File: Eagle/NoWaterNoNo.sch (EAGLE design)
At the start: 13 parts, among them U2 TINY85-20-DIP

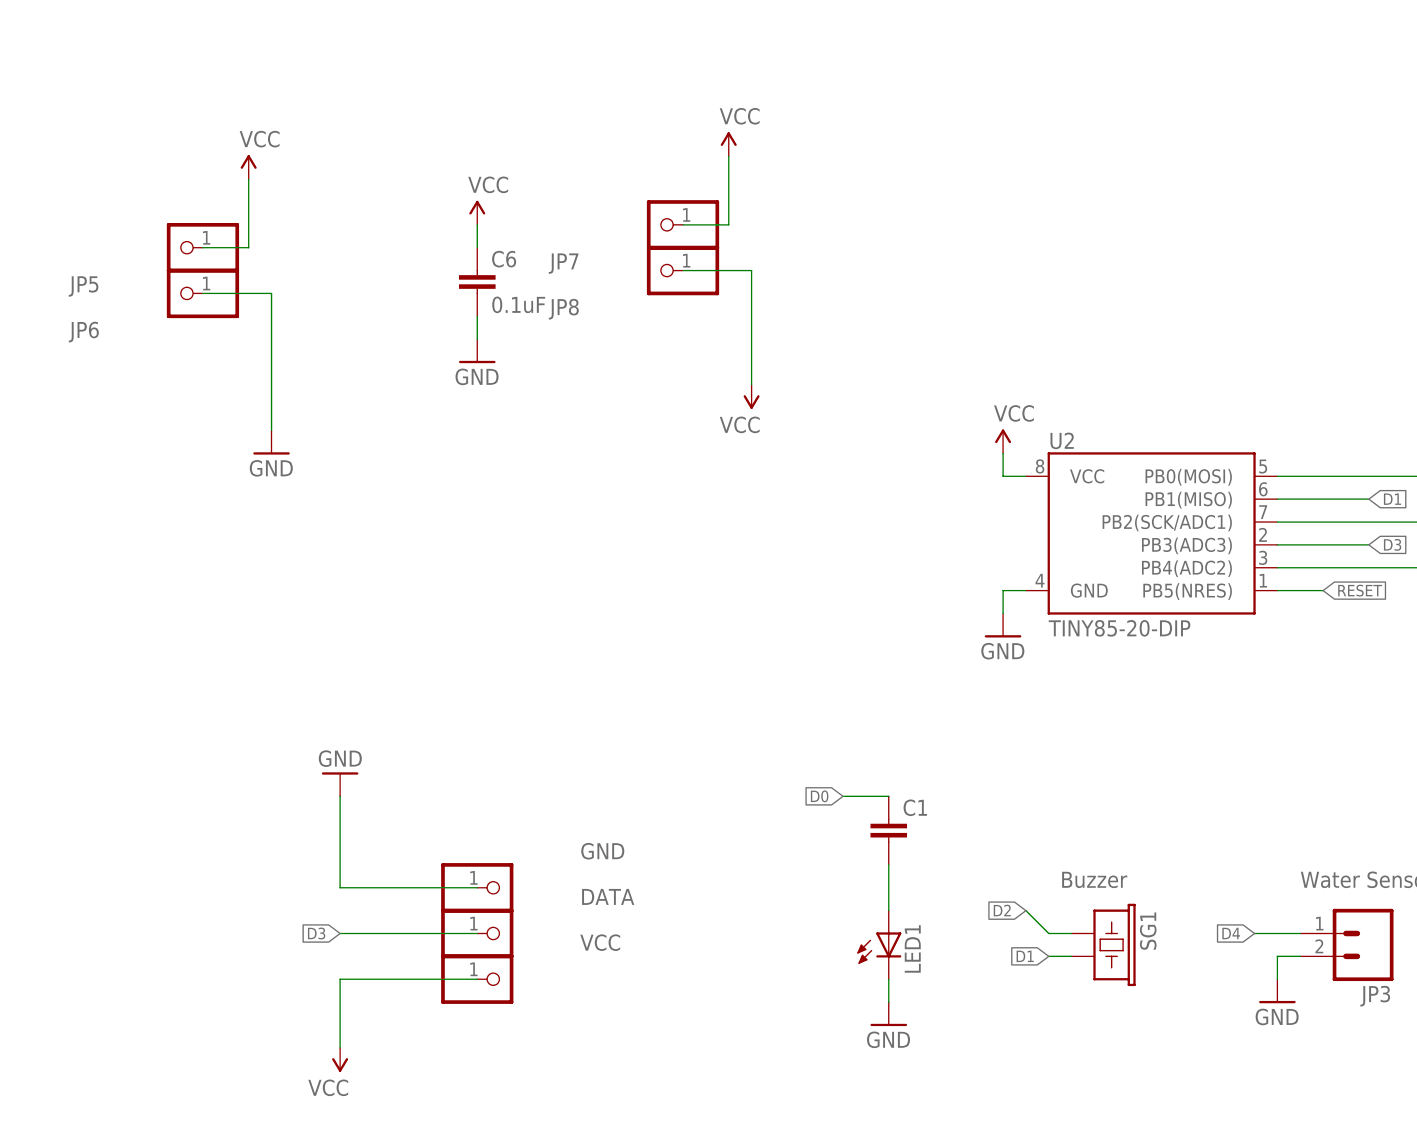
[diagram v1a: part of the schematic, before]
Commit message: Changed board layout. Buzzer, radio and sensor have changed pin assignments.
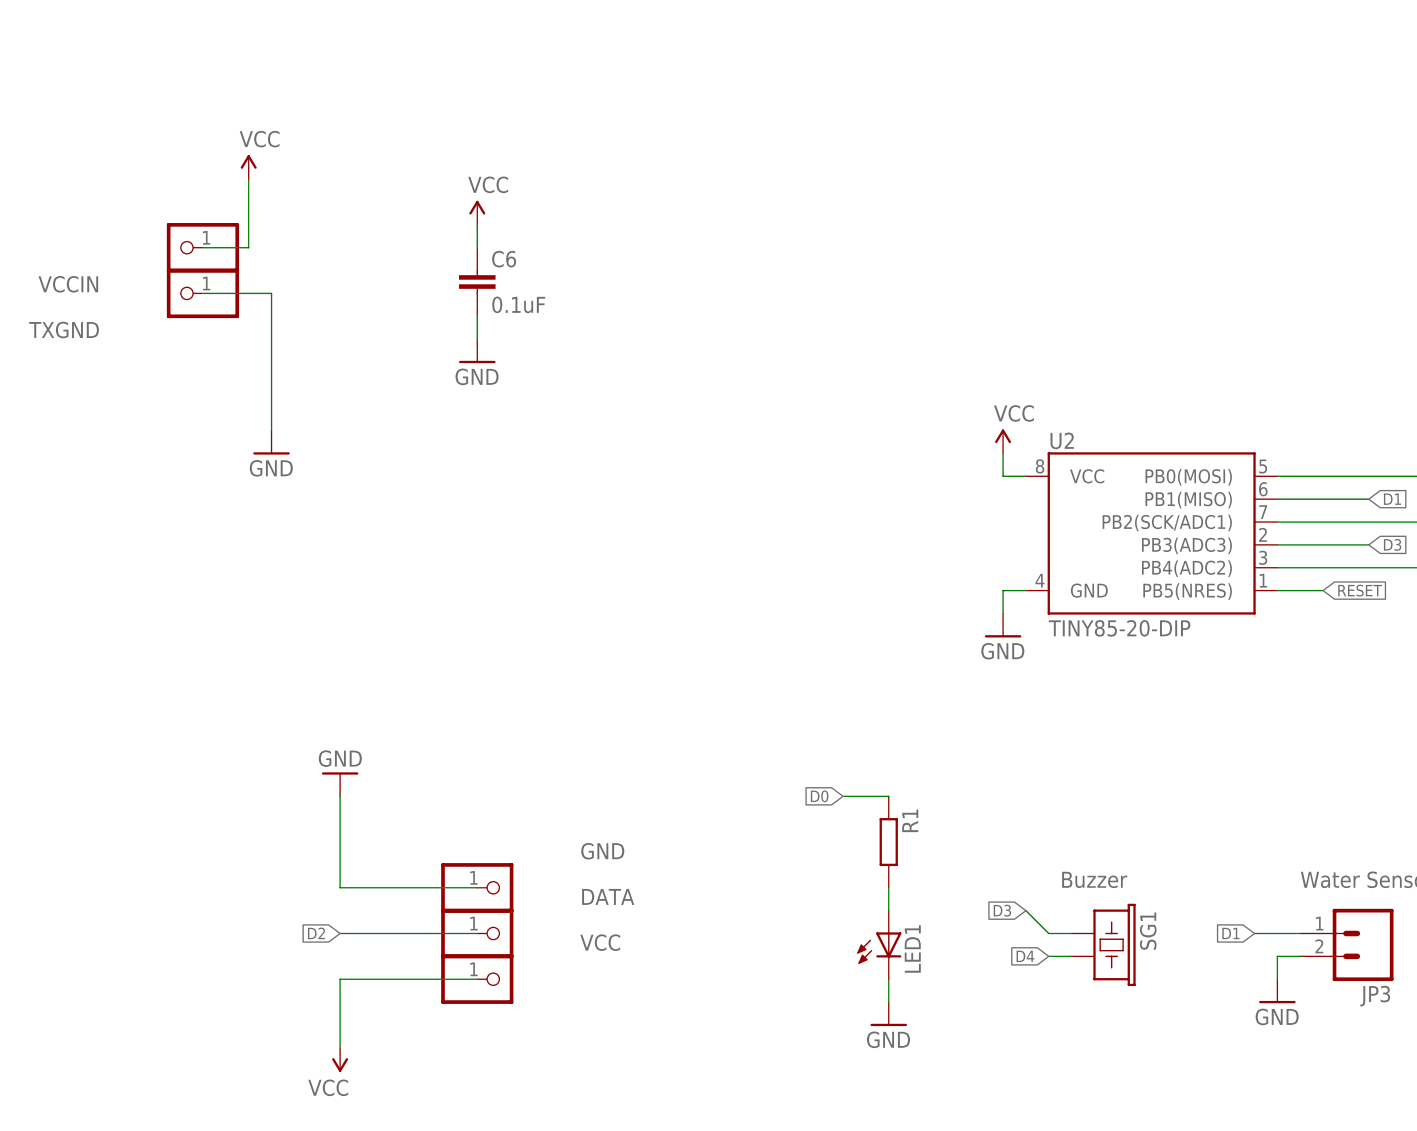
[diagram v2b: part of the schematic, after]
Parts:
- removed C1: (no value), resistor:C-EU025-025X050
- removed JP7, JP8: (no value), pinhead:PINHD-1X1
- added R1: (no value), rcl:R-EU_0204/2V
- renumbered JP5 to VCCIN, JP6 to TXGND
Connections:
- net D0: now also R1.1; no longer C1.1
- net D1: now also JP3.1; no longer SG1.2
- net D2: now also DATA.1; no longer SG1.1
- net D3: now also SG1.1; no longer DATA.1
- net D4: now also SG1.2; no longer JP3.1
- net N$1: now also R1.2; no longer C1.2
- net VCC: no longer JP7.1, JP8.1
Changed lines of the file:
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@@
 <part name="GND1" library="SparkFun" deviceset="GND" device=""/>
 <part name="P+1" library="SparkFun" deviceset="VCC" device=""/>
-<part name="JP5" library="pinhead" deviceset="PINHD-1X1" device=""/>
-<part name="JP6" library="pinhead" deviceset="PINHD-1X1" device=""/>
-<part name="P+4" library="SparkFun" deviceset="VCC" device=""/>
-<part name="JP7" library="pinhead" deviceset="PINHD-1X1" device=""/>
-<part name="JP8" library="pinhead" deviceset="PINHD-1X1" device=""/>
-<part name="P+6" library="SparkFun" deviceset="VCC" device=""/>
-<part name="C1" library="resistor" deviceset="C-EU" device="025-025X050"/>
+<part name="VCCIN" library="pinhead" deviceset="PINHD-1X1" device=""/>
+<part name="TXGND" library="pinhead" deviceset="PINHD-1X1" device=""/>
+<part name="R1" library="rcl" deviceset="R-EU_" device="0204/2V"/>
 </parts>
 <sheets>
@@
 <instance part="GND1" gate="1" x="48.26" y="99.06" rot="R180"/>
 <instance part="P+1" gate="1" x="48.26" y="68.58" rot="R180"/>
-<instance part="JP5" gate="G$1" x="30.48" y="157.48" smashed="yes" rot="R180">
+<instance part="VCCIN" gate="G$1" x="30.48" y="157.48" smashed="yes" rot="R180">
 <attribute name="NAME" x="21.59" y="154.305" size="1.778" layer="95" rot="R180"/>
 <attribute name="VALUE" x="36.83" y="162.56" size="1.778" layer="96" rot="R180"/>
 </instance>
-<instance part="JP6" gate="G$1" x="30.48" y="152.4" smashed="yes" rot="R180">
+<instance part="TXGND" gate="G$1" x="30.48" y="152.4" smashed="yes" rot="R180">
 <attribute name="NAME" x="21.59" y="149.225" size="1.778" layer="95" rot="R180"/>
 <attribute name="VALUE" x="36.83" y="157.48" size="1.778" layer="96" rot="R180"/>
 </instance>
-<instance part="P+4" gate="1" x="91.44" y="167.64"/>
-<instance part="JP7" gate="G$1" x="83.82" y="160.02" smashed="yes" rot="R180">
-<attribute name="NAME" x="74.93" y="156.845" size="1.778" layer="95" rot="R180"/>
-<attribute name="VALUE" x="90.17" y="165.1" size="1.778" layer="96" rot="R180"/>
-</instance>
-<instance part="JP8" gate="G$1" x="83.82" y="154.94" smashed="yes" rot="R180">
-<attribute name="NAME" x="74.93" y="151.765" size="1.778" layer="95" rot="R180"/>
-<attribute name="VALUE" x="90.17" y="160.02" size="1.778" layer="96" rot="R180"/>
-</instance>
-<instance part="P+6" gate="1" x="93.98" y="142.24" rot="R180"/>
-<instance part="C1" gate="G$1" x="109.22" y="93.98"/>
+<instance part="R1" gate="G$1" x="109.22" y="91.44" rot="R270"/>
 </instances>
 <busses>
@@
 <segment>
 <pinref part="GND7" gate="1" pin="GND"/>
-<pinref part="JP6" gate="G$1" pin="1"/>
+<pinref part="TXGND" gate="G$1" pin="1"/>
 <wire x1="33.02" y1="152.4" x2="40.64" y2="152.4" width="0.1524" layer="91"/>
 <wire x1="40.64" y1="152.4" x2="40.64" y2="137.16" width="0.1524" layer="91"/>
@@
 <pinref part="P+2" gate="1" pin="VCC"/>
 <wire x1="38.1" y1="165.1" x2="38.1" y2="157.48" width="0.1524" layer="91"/>
-<pinref part="JP5" gate="G$1" pin="1"/>
+<pinref part="VCCIN" gate="G$1" pin="1"/>
 <wire x1="38.1" y1="157.48" x2="33.02" y2="157.48" width="0.1524" layer="91"/>
 </segment>
@@
 <wire x1="48.26" y1="76.2" x2="48.26" y2="68.58" width="0.1524" layer="91"/>
 </segment>
-<segment>
-<pinref part="P+4" gate="1" pin="VCC"/>
-<wire x1="91.44" y1="167.64" x2="91.44" y2="160.02" width="0.1524" layer="91"/>
-<pinref part="JP7" gate="G$1" pin="1"/>
-<wire x1="91.44" y1="160.02" x2="86.36" y2="160.02" width="0.1524" layer="91"/>
-</segment>
-<segment>
-<pinref part="JP8" gate="G$1" pin="1"/>
-<wire x1="86.36" y1="154.94" x2="93.98" y2="154.94" width="0.1524" layer="91"/>
-<wire x1="93.98" y1="154.94" x2="93.98" y2="142.24" width="0.1524" layer="91"/>
-<pinref part="P+6" gate="1" pin="VCC"/>
-</segment>
 </net>
 <net name="RESET" class="0">
@@
 <net name="D4" class="0">
 <segment>
-<pinref part="JP3" gate="G$1" pin="1"/>
-<wire x1="154.94" y1="81.28" x2="149.86" y2="81.28" width="0.1524" layer="91"/>
-<label x="149.86" y="81.28" size="1.27" layer="95" rot="R180" xref="yes"/>
-</segment>
-<segment>
 <pinref part="U2" gate="G$1" pin="PB4(ADC2)"/>
 <wire x1="152.4" y1="121.92" x2="170.18" y2="121.92" width="0.1524" layer="91"/>
 <label x="170.18" y="121.92" size="1.27" layer="95" xref="yes"/>
 </segment>
+<segment>
+<pinref part="SG1" gate="G$1" pin="2"/>
+<wire x1="129.54" y1="78.74" x2="127" y2="78.74" width="0.1524" layer="91"/>
+<label x="127" y="78.74" size="1.27" layer="95" rot="R180" xref="yes"/>
+</segment>
 </net>
 <net name="D0" class="0">
@@
 <label x="104.14" y="96.52" size="1.27" layer="95" rot="R180" xref="yes"/>
 <wire x1="104.14" y1="96.52" x2="109.22" y2="96.52" width="0.1524" layer="91"/>
-<pinref part="C1" gate="G$1" pin="1"/>
-</segment>
-</net>
-<net name="D1" class="0">
-<segment>
-<pinref part="SG1" gate="G$1" pin="2"/>
-<wire x1="129.54" y1="78.74" x2="127" y2="78.74" width="0.1524" layer="91"/>
-<label x="127" y="78.74" size="1.27" layer="95" rot="R180" xref="yes"/>
-</segment>
-<segment>
-<pinref part="U2" gate="G$1" pin="PB1(MISO)"/>
-<wire x1="152.4" y1="129.54" x2="162.56" y2="129.54" width="0.1524" layer="91"/>
-<label x="162.56" y="129.54" size="1.27" layer="95" xref="yes"/>
-</segment>
-</net>
-<net name="D2" class="0">
-<segment>
-<pinref part="U2" gate="G$1" pin="PB2(SCK/ADC1)"/>
-<wire x1="152.4" y1="127" x2="170.18" y2="127" width="0.1524" layer="91"/>
-<label x="170.18" y="127" size="1.27" layer="95" xref="yes"/>
+<pinref part="R1" gate="G$1" pin="1"/>
+</segment>
+</net>
+<net name="D3" class="0">
+<segment>
+<pinref part="U2" gate="G$1" pin="PB3(ADC3)"/>
+<wire x1="152.4" y1="124.46" x2="162.56" y2="124.46" width="0.1524" layer="91"/>
+<label x="162.56" y="124.46" size="1.27" layer="95" xref="yes"/>
 </segment>
 <segment>
@@
 </segment>
 </net>
-<net name="D3" class="0">
-<segment>
-<pinref part="U2" gate="G$1" pin="PB3(ADC3)"/>
-<wire x1="152.4" y1="124.46" x2="162.56" y2="124.46" width="0.1524" layer="91"/>
-<label x="162.56" y="124.46" size="1.27" layer="95" xref="yes"/>
+<net name="N$1" class="0">
+<segment>
+<pinref part="R1" gate="G$1" pin="2"/>
+<pinref part="LED1" gate="G$1" pin="A"/>
+<wire x1="109.22" y1="86.36" x2="109.22" y2="83.82" width="0.1524" layer="91"/>
+</segment>
+</net>
+<net name="D1" class="0">
+<segment>
+<pinref part="U2" gate="G$1" pin="PB1(MISO)"/>
+<wire x1="152.4" y1="129.54" x2="162.56" y2="129.54" width="0.1524" layer="91"/>
+<label x="162.56" y="129.54" size="1.27" layer="95" xref="yes"/>
+</segment>
+<segment>
+<pinref part="JP3" gate="G$1" pin="1"/>
+<wire x1="154.94" y1="81.28" x2="149.86" y2="81.28" width="0.1524" layer="91"/>
+<label x="149.86" y="81.28" size="1.27" layer="95" rot="R180" xref="yes"/>
+</segment>
+</net>
+<net name="D2" class="0">
+<segment>
+<pinref part="U2" gate="G$1" pin="PB2(SCK/ADC1)"/>
+<wire x1="152.4" y1="127" x2="170.18" y2="127" width="0.1524" layer="91"/>
+<label x="170.18" y="127" size="1.27" layer="95" xref="yes"/>
 </segment>
 <segment>
@@
 </segment>
 </net>
-<net name="N$1" class="0">
-<segment>
-<pinref part="C1" gate="G$1" pin="2"/>
-<pinref part="LED1" gate="G$1" pin="A"/>
-<wire x1="109.22" y1="88.9" x2="109.22" y2="83.82" width="0.1524" layer="91"/>
-</segment>
-</net>

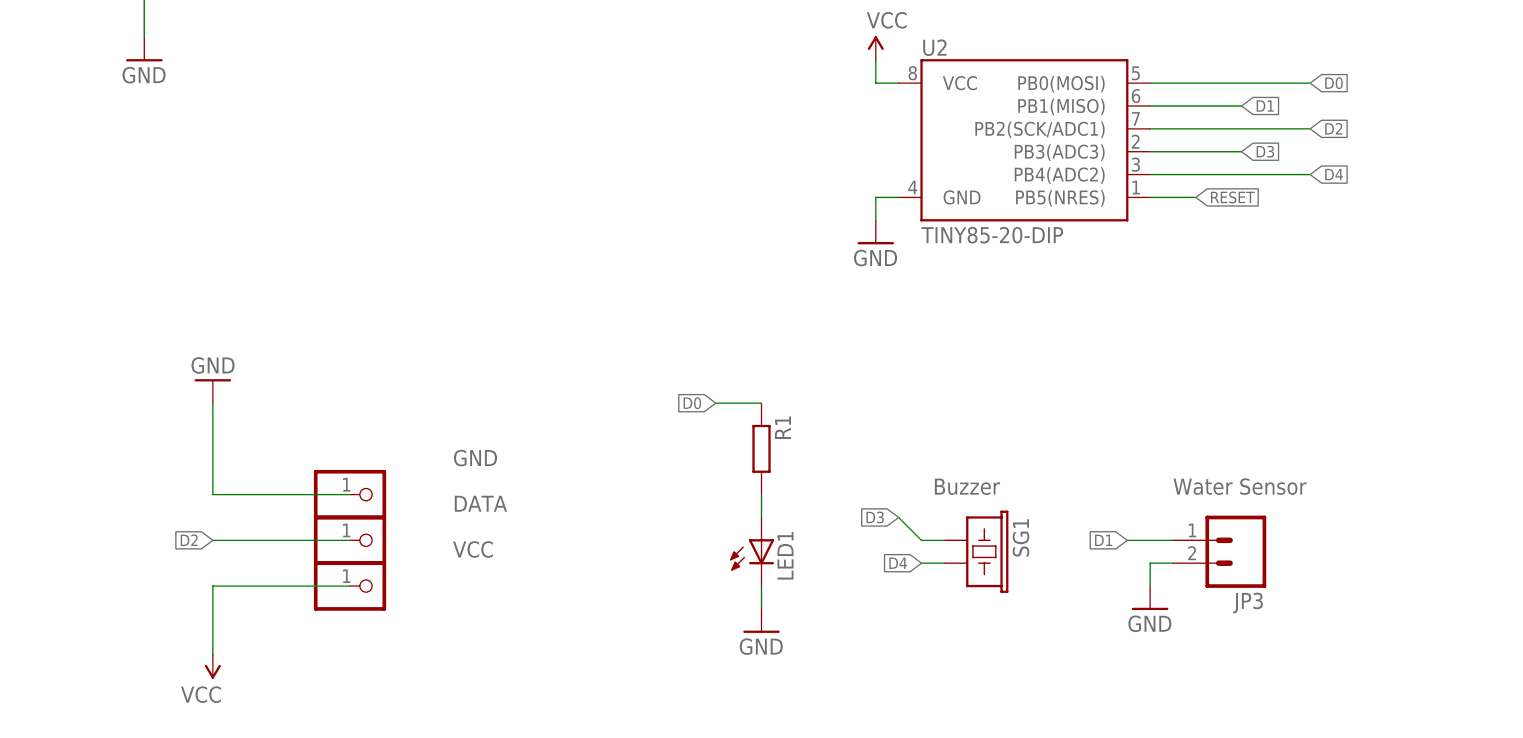
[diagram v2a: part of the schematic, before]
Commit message: Changed board layouts once again. Changes made to Arduino code as well.
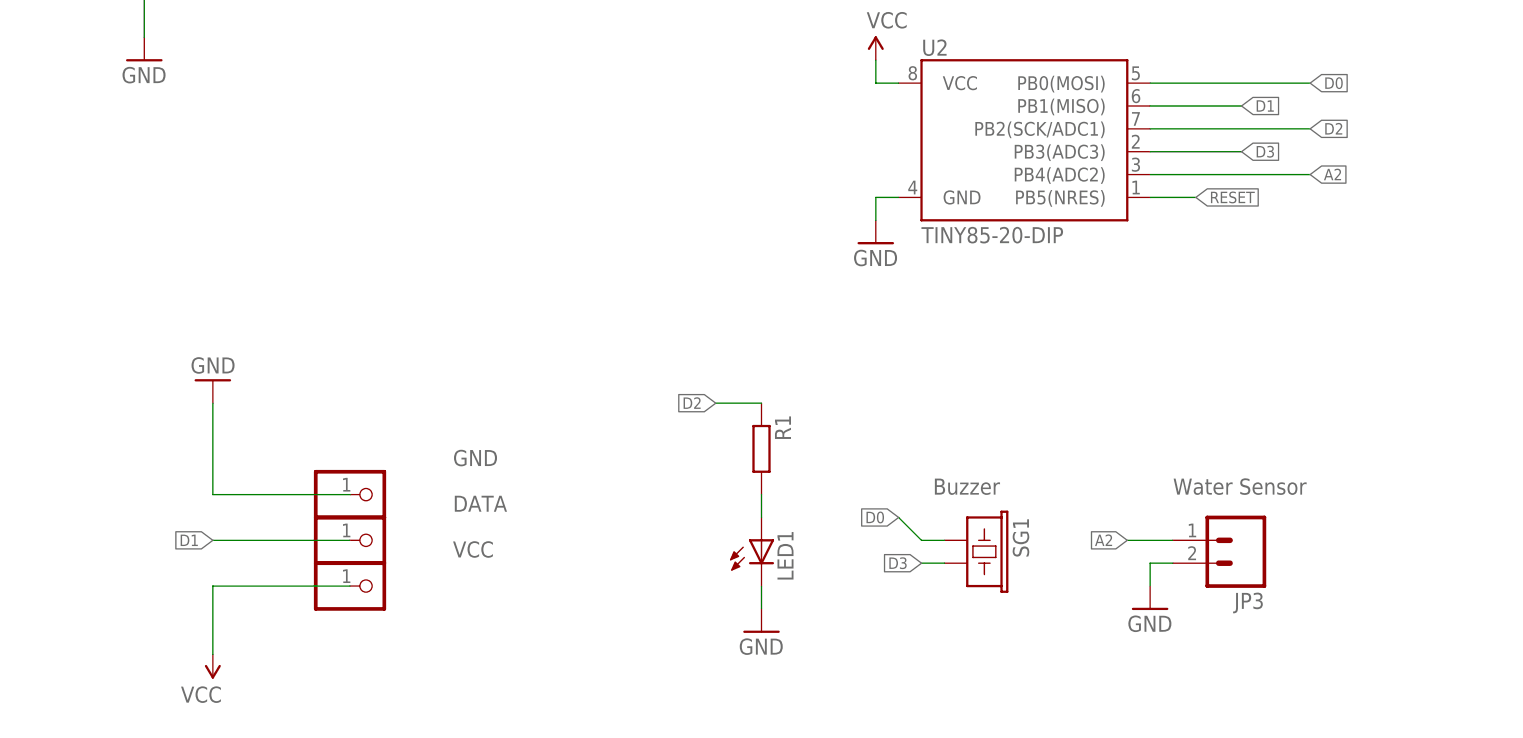
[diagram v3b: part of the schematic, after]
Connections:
- removed net D4: SG1.2, U2.PB4(ADC2)
- new net A2: JP3.1, U2.PB4(ADC2)
- net D0: now also SG1.1; no longer R1.1
- net D1: now also DATA.1; no longer JP3.1
- net D2: now also R1.1; no longer DATA.1
- net D3: now also SG1.2; no longer SG1.1
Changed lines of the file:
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@@
-</segment>
-</net>
-<net name="D4" class="0">
-<segment>
-<pinref part="U2" gate="G$1" pin="PB4(ADC2)"/>
-<wire x1="152.4" y1="121.92" x2="170.18" y2="121.92" width="0.1524" layer="91"/>
-<label x="170.18" y="121.92" size="1.27" layer="95" xref="yes"/>
-</segment>
-<segment>
-<pinref part="SG1" gate="G$1" pin="2"/>
-<wire x1="129.54" y1="78.74" x2="127" y2="78.74" width="0.1524" layer="91"/>
-<label x="127" y="78.74" size="1.27" layer="95" rot="R180" xref="yes"/>
 </segment>
 </net>
@@
 </segment>
 <segment>
-<label x="104.14" y="96.52" size="1.27" layer="95" rot="R180" xref="yes"/>
-<wire x1="104.14" y1="96.52" x2="109.22" y2="96.52" width="0.1524" layer="91"/>
-<pinref part="R1" gate="G$1" pin="1"/>
+<pinref part="SG1" gate="G$1" pin="1"/>
+<wire x1="129.54" y1="81.28" x2="127" y2="81.28" width="0.1524" layer="91"/>
+<label x="124.46" y="83.82" size="1.27" layer="95" rot="R180" xref="yes"/>
+<wire x1="127" y1="81.28" x2="124.46" y2="83.82" width="0.1524" layer="91"/>
 </segment>
 </net>
@@
 </segment>
 <segment>
-<pinref part="SG1" gate="G$1" pin="1"/>
-<wire x1="129.54" y1="81.28" x2="127" y2="81.28" width="0.1524" layer="91"/>
-<label x="124.46" y="83.82" size="1.27" layer="95" rot="R180" xref="yes"/>
-<wire x1="127" y1="81.28" x2="124.46" y2="83.82" width="0.1524" layer="91"/>
+<pinref part="SG1" gate="G$1" pin="2"/>
+<wire x1="129.54" y1="78.74" x2="127" y2="78.74" width="0.1524" layer="91"/>
+<label x="127" y="78.74" size="1.27" layer="95" rot="R180" xref="yes"/>
 </segment>
 </net>
@@
 </segment>
 <segment>
-<pinref part="JP3" gate="G$1" pin="1"/>
-<wire x1="154.94" y1="81.28" x2="149.86" y2="81.28" width="0.1524" layer="91"/>
-<label x="149.86" y="81.28" size="1.27" layer="95" rot="R180" xref="yes"/>
+<pinref part="DATA" gate="G$1" pin="1"/>
+<wire x1="63.5" y1="81.28" x2="48.26" y2="81.28" width="0.1524" layer="91"/>
+<label x="48.26" y="81.28" size="1.27" layer="95" rot="R180" xref="yes"/>
 </segment>
 </net>
@@
 </segment>
 <segment>
-<pinref part="DATA" gate="G$1" pin="1"/>
-<wire x1="63.5" y1="81.28" x2="48.26" y2="81.28" width="0.1524" layer="91"/>
-<label x="48.26" y="81.28" size="1.27" layer="95" rot="R180" xref="yes"/>
+<label x="104.14" y="96.52" size="1.27" layer="95" rot="R180" xref="yes"/>
+<wire x1="104.14" y1="96.52" x2="109.22" y2="96.52" width="0.1524" layer="91"/>
+<pinref part="R1" gate="G$1" pin="1"/>
 </segment>
 </net>
+<net name="A2" class="0">
+<segment>
+<pinref part="JP3" gate="G$1" pin="1"/>
+<wire x1="154.94" y1="81.28" x2="149.86" y2="81.28" width="0.1524" layer="91"/>
+<label x="149.86" y="81.28" size="1.27" layer="95" rot="R180" xref="yes"/>
+</segment>
+<segment>
+<pinref part="U2" gate="G$1" pin="PB4(ADC2)"/>
+<wire x1="152.4" y1="121.92" x2="170.18" y2="121.92" width="0.1524" layer="91"/>
+<label x="170.18" y="121.92" size="1.27" layer="95" xref="yes"/>
+</segment>
+</net>
